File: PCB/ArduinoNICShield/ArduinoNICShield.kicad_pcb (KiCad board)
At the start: 2 copper layers, 4 parts, among them Q1 PN2222A

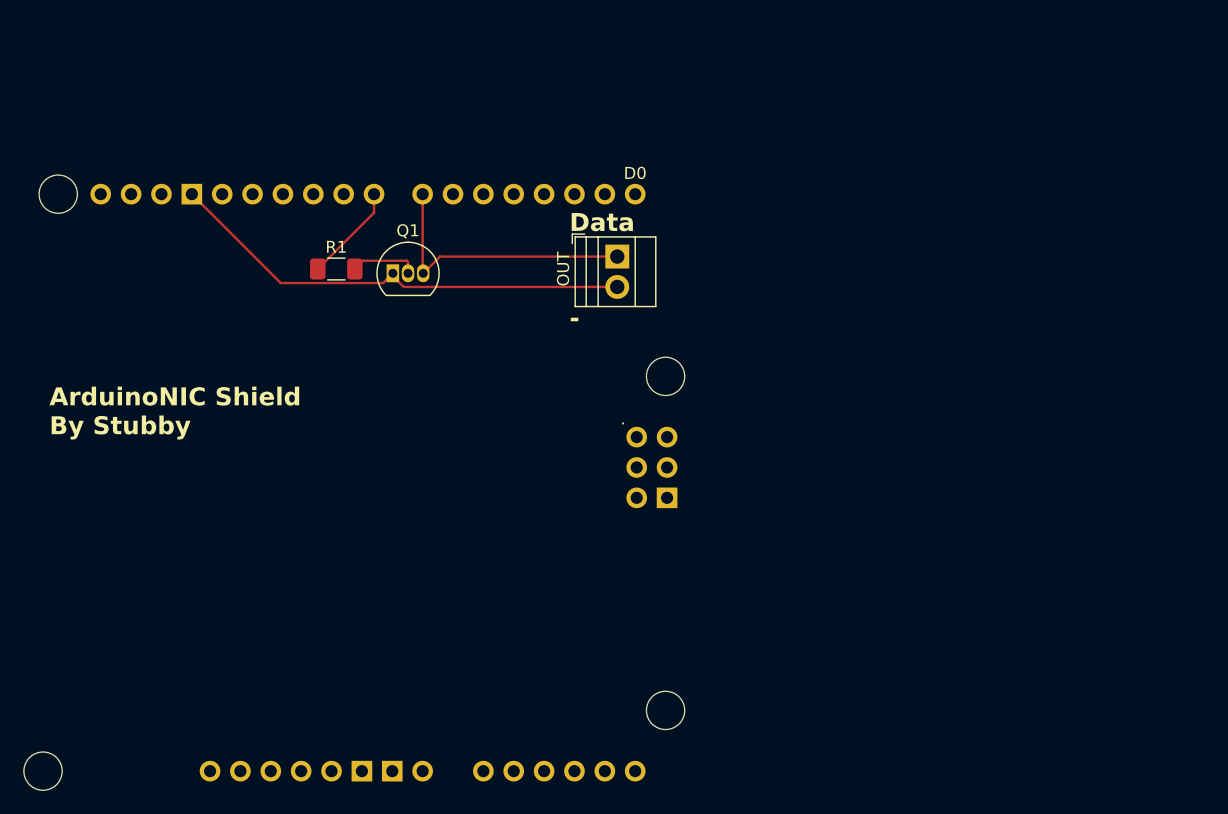
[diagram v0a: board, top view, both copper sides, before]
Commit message: Correction of the arduino library, and start of the implementation of the python interface
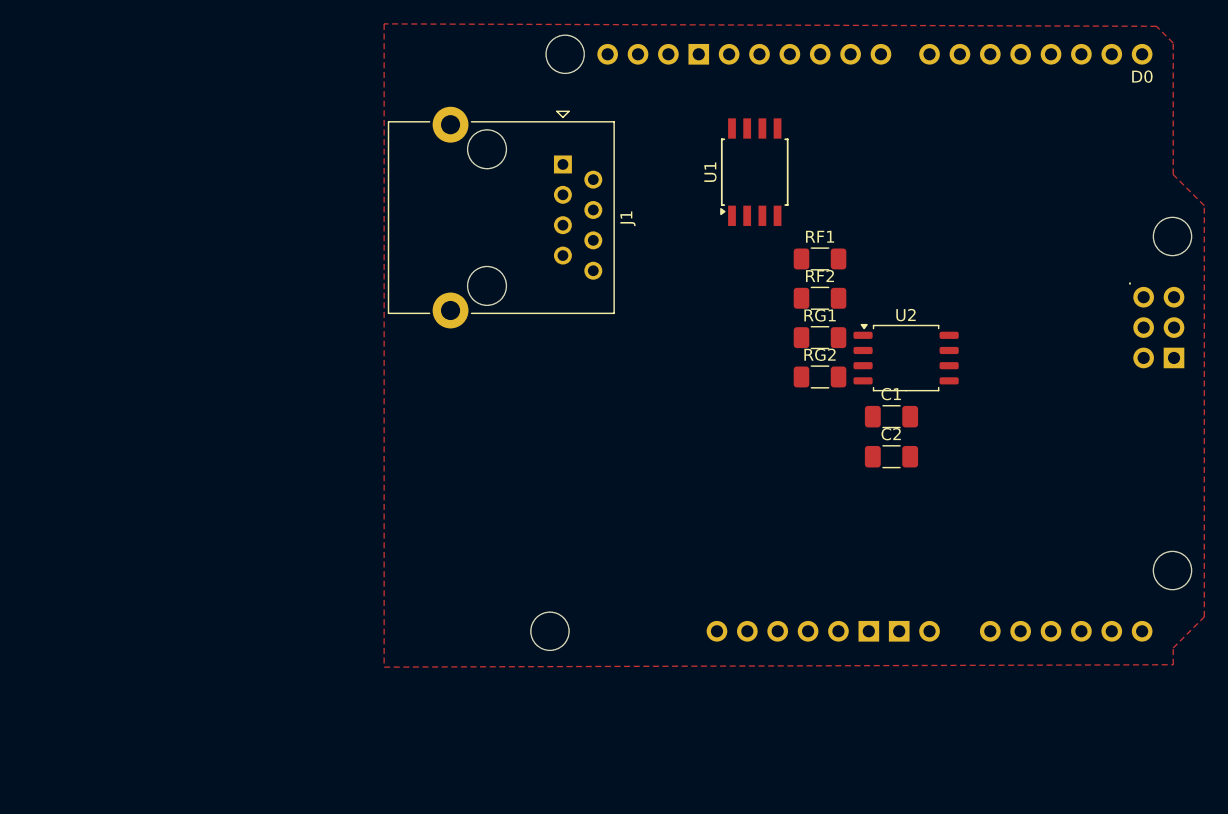
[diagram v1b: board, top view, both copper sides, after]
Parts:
- removed OUT: OUT, TerminalBlock:TerminalBlock_Xinya_XY308-2.54-2P_1x02_P2.54mm_Horizontal
- removed Q1: PN2222A, Package_TO_SOT_THT:TO-92_Inline
- removed R1: 120K, Resistor_SMD:R_1206_3216Metric_Pad1.30x1.75mm_HandSolder
- added C1: 10uF, Capacitor_SMD:C_1206_3216Metric_Pad1.33x1.80mm_HandSolder, F.Cu at (186.4, 83.8)
- added C2: 10uF, Capacitor_SMD:C_1206_3216Metric_Pad1.33x1.80mm_HandSolder, F.Cu at (186.4, 87.2)
- added J1: RJ45, Connector_RJ:RJ45_Ninigi_GE, F.Cu at (159.0, 62.8)
- added RF1: R, Resistor_SMD:R_1206_3216Metric_Pad1.30x1.75mm_HandSolder, F.Cu at (180.5, 70.7)
- added RF2: R, Resistor_SMD:R_1206_3216Metric_Pad1.30x1.75mm_HandSolder, F.Cu at (180.5, 74.0)
- added RG1: R, Resistor_SMD:R_1206_3216Metric_Pad1.30x1.75mm_HandSolder, F.Cu at (180.5, 77.2)
- added RG2: R, Resistor_SMD:R_1206_3216Metric_Pad1.30x1.75mm_HandSolder, F.Cu at (180.5, 80.5)
- added U1: THS4531ID, Package_SO:SOIC-8W_5.3x5.3mm_P1.27mm, F.Cu at (175.0, 63.4)
- added U2: ICL7660, Package_SO:SOIC-8_5.23x5.23mm_P1.27mm, F.Cu at (187.7, 79.0)
- moved A1 44.0 mm to (143.9, 104.3)
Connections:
- A1 pad 5V1: unconnected-(A1-5V-Pad5V1) -> VCC
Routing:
- net GND: track 39.6 -> 0.00 mm
- net RX_Arduino: track 23.5 -> 0.00 mm
- net TX_Arduino: track 8.21 -> 0.00 mm
- net Net-(Q1-B): track 5.73 -> 0.00 mm
- added copper zone on F.Cu, net GND
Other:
- board text removed: "-"
- board text removed: "ArduinoNIC Shield By Stubby"
- board text removed: "Data"
